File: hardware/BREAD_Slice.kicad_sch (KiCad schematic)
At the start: 15 parts, among them J1 Conn_01x10_Female, J2 I2C_01x04

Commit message: Initial commit
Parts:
- removed C1, C3, C4: 22uF, Capacitor_SMD:C_1206_3216Metric, symbol Device:C_Small
- removed C2: 100nF, Capacitor_SMD:C_1206_3216Metric, symbol Device:C_Small
- removed D1: WS2812B_5050, SparkFun-LED:WS2812-5050-4PIN, symbol SparkFun-LED:WS2812B_5050
- removed HS1: Heatsink_Pad, SparkFun-Fuse:Thermal Pad, symbol Mechanical:Heatsink_Pad
- removed J2: I2C_01x04, Connector_JST:JST_SH_SM04B-SRSS-TB_1x04-1MP_P1.00mm_Horizontal, symbol SparkFun-Connector:I2C_01x04
- removed L1: 4.7uH, Inductor_SMD:L_1210_3225Metric, symbol Device:L_Small
- removed U1: ~, Package_TO_SOT_SMD:TSOT-23-6, symbol SparkFun-DiscreteSemi:AP63205
- added C1, C2: 10uF_t, OCI_UPL_FOOTPRINTS:C_2312, symbol BREAD_Slice-rescue:10uF_t-OCI_UPL_2_Capacitors
- added J2, J3, J4, J5: Screw_Terminal_01x02, TerminalBlock_TE-Connectivity:TerminalBlock_TE_282834-2_1x02_P2.54mm_Horizontal, symbol Connector:Screw_Terminal_01x02
- added Logo1: Logo_Open_Hardware_Small, Symbol:OSHW-Symbol_6.7x6mm_SilkScreen, symbol Graphic:Logo_Open_Hardware_Small
- added U1, U2, U3, U4: ACS723xMATR-10AB, Package_SO:SOIC-16W_7.5x10.3mm_P1.27mm, symbol Sensor_Current:ACS723xMATR-10AB
- H1, H4: footprint MountingHole:MountingHole_5mm -> MountingHole:MountingHole_3.2mm_M3_DIN965_Pad
- H2: renamed from H3; footprint MountingHole:MountingHole_5mm -> MountingHole:MountingHole_3.2mm_M3_DIN965_Pad
- H3: renamed from H2; footprint MountingHole:MountingHole_5mm -> MountingHole:MountingHole_3.2mm_M3_DIN965_Pad
- J1: symbol Connector:Conn_01x10_Female -> BREAD_Slice-rescue:Conn_01x10_Female-Connector
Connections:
- net +12V: now also A1.30 (VIN), C1.1
- net +5V: now also C2.1, U1.10 (VCC), U2.10 (VCC), U3.10 (VCC), U4.10 (VCC)
- net GND: now also C1.2, C2.2, U1.11 (NC), U1.13 (BW_SEL), U1.14 (NC), U1.15 (GND), U2.11 (NC), U2.13 (BW_SEL), U2.14 (NC), U2.15 (GND), U3.11 (NC), U3.13 (BW_SEL), U3.14 (NC), U3.15 (GND), U4.11 (NC), U4.13 (BW_SEL), U4.14 (NC), U4.15 (GND)
- net CURR1: now reaches A1.19 (A0)
- net CURR1: now also U1.12 (VIOUT)
- net CURR2: now reaches A1.20 (A1)
- net CURR2: now also U3.12 (VIOUT)
- net CURR3: now reaches A1.21 (A2)
- net CURR3: now also U2.12 (VIOUT)
- net CURR4: now reaches A1.22 (A3)
- net CURR4: now also U4.12 (VIOUT)
- net LED: no longer names the net of A1.8 (D5)
- new net: J2.2 (Pin_2), U1.1 (IP+), U1.2 (IP+), U1.3 (IP+), U1.4 (IP+)
- new net: J2.1 (Pin_1), U1.5 (IP-), U1.6 (IP-), U1.7 (IP-), U1.8 (IP-)
- new net: J4.2 (Pin_2), U3.1 (IP+), U3.2 (IP+), U3.3 (IP+), U3.4 (IP+)
- new net: J4.1 (Pin_1), U3.5 (IP-), U3.6 (IP-), U3.7 (IP-), U3.8 (IP-)
- new net: J3.2 (Pin_2), U2.1 (IP+), U2.2 (IP+), U2.3 (IP+), U2.4 (IP+)
- new net: J3.1 (Pin_1), U2.5 (IP-), U2.6 (IP-), U2.7 (IP-), U2.8 (IP-)
- new net: J5.2 (Pin_2), U4.1 (IP+), U4.2 (IP+), U4.3 (IP+), U4.4 (IP+)
- new net: J5.1 (Pin_1), U4.5 (IP-), U4.6 (IP-), U4.7 (IP-), U4.8 (IP-)
- no-connect marks 22 -> 17
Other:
- moved on the sheet: A1, H1, H2, H3, H4, J1

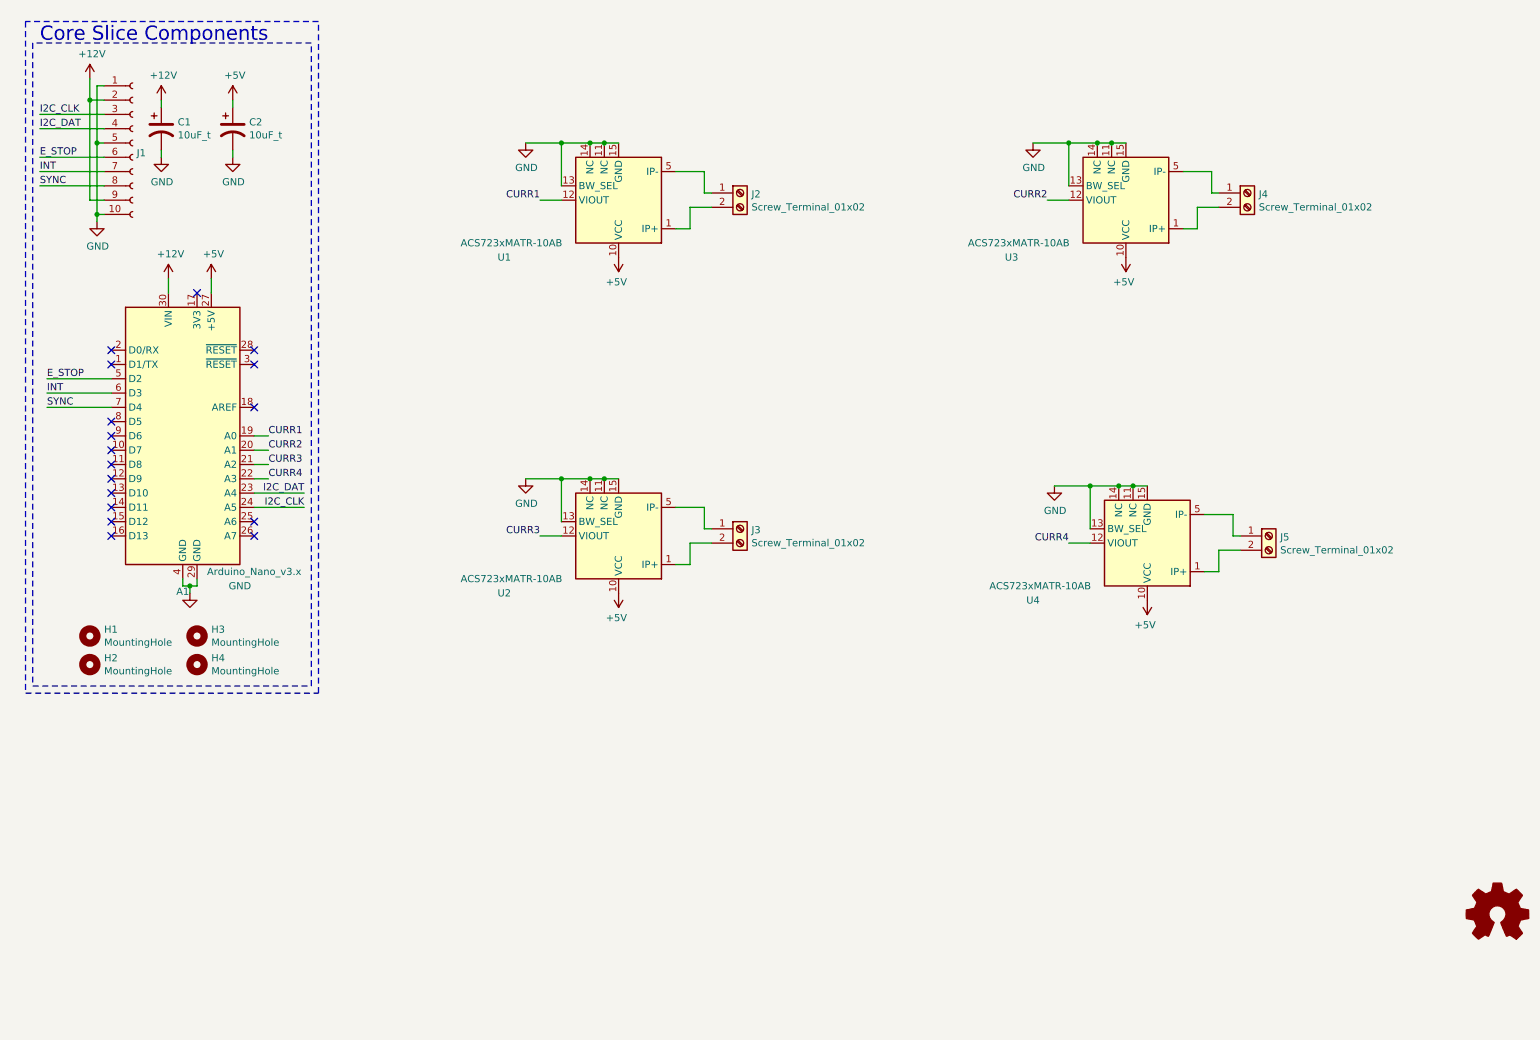
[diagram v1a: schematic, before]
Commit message: updated to new BREAD format
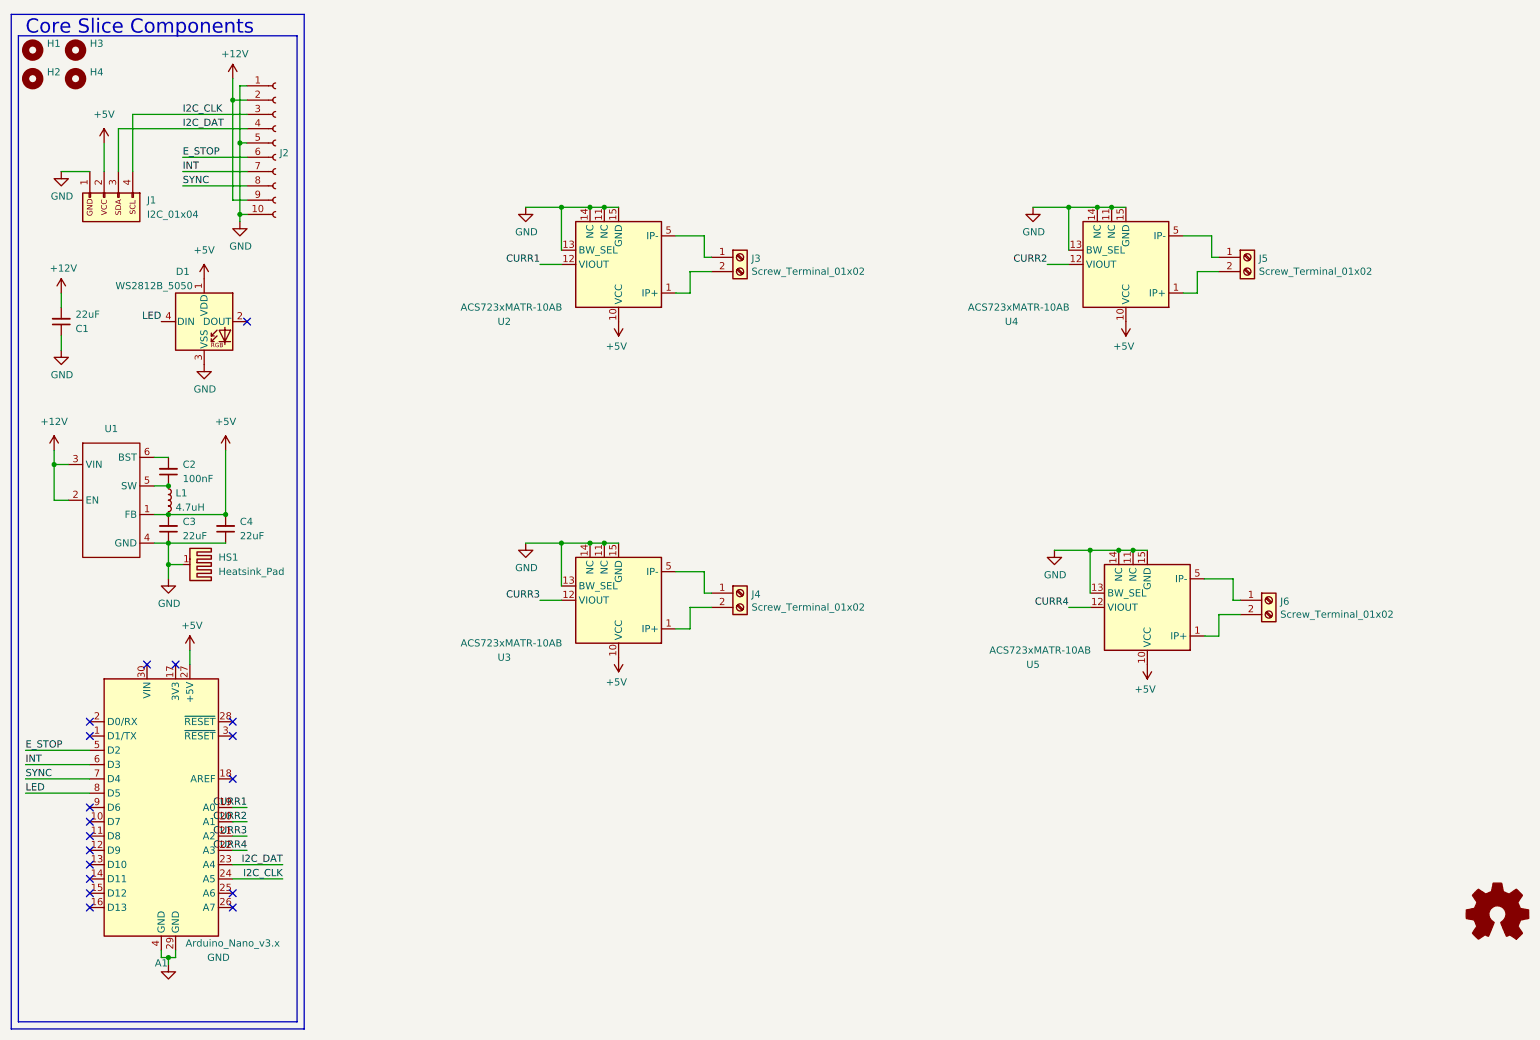
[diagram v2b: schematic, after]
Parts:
- removed C1, C2: 10uF_t, OCI_UPL_FOOTPRINTS:C_2312, symbol BREAD_Slice-rescue:10uF_t-OCI_UPL_2_Capacitors
- removed J2: Screw_Terminal_01x02, TerminalBlock_TE-Connectivity:TerminalBlock_TE_282834-2_1x02_P2.54mm_Horizontal, symbol Connector:Screw_Terminal_01x02
- removed Logo1: Logo_Open_Hardware_Small, Symbol:OSHW-Symbol_6.7x6mm_SilkScreen, symbol Graphic:Logo_Open_Hardware_Small
- removed U1: ACS723xMATR-10AB, Package_SO:SOIC-16W_7.5x10.3mm_P1.27mm, symbol Sensor_Current:ACS723xMATR-10AB
- added C1, C3, C4: 22uF, Capacitor_SMD:C_1206_3216Metric, symbol Device:C_Small
- added C2: 100nF, Capacitor_SMD:C_1206_3216Metric, symbol Device:C_Small
- added D1: WS2812B_5050, SparkFun-LED:WS2812-5050-4PIN, symbol SparkFun-LED:WS2812B_5050
- added HS1: Heatsink_Pad, KML-Custom:Thermal Pad, symbol Mechanical:Heatsink_Pad
- added J1: I2C_01x04, Connector_JST:JST_SH_SM04B-SRSS-TB_1x04-1MP_P1.00mm_Horizontal, symbol SparkFun-Connector:I2C_01x04
- added J6: Screw_Terminal_01x02, TerminalBlock_TE-Connectivity:TerminalBlock_TE_282834-2_1x02_P2.54mm_Horizontal, symbol Connector:Screw_Terminal_01x02
- added L1: 4.7uH, Inductor_SMD:L_1210_3225Metric, symbol Device:L_Small
- added U1: ~, Package_TO_SOT_SMD:TSOT-23-6, symbol SparkFun-DiscreteSemi:AP63205
- added U5: ACS723xMATR-10AB, Package_SO:SOIC-16W_7.5x10.3mm_P1.27mm, symbol Sensor_Current:ACS723xMATR-10AB
- H1, H4: footprint MountingHole:MountingHole_3.2mm_M3_DIN965_Pad -> MountingHole:MountingHole_5mm
- H2: renamed from H3; footprint MountingHole:MountingHole_3.2mm_M3_DIN965_Pad -> MountingHole:MountingHole_5mm
- H3: renamed from H2; footprint MountingHole:MountingHole_3.2mm_M3_DIN965_Pad -> MountingHole:MountingHole_5mm
- J2: renamed from J1; symbol BREAD_Slice-rescue:Conn_01x10_Female-Connector -> Connector:Conn_01x10_Female
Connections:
- net +12V: now also C1.2, U1.2 (EN), U1.3 (VIN); no longer A1.30 (VIN)
- net +5V: now also C3.2, C4.2, D1.1 (VDD), J1.2 (Pin_2), L1.2, U1.1 (FB), U5.10 (VCC)
- net CURR1: now also U2.12 (VIOUT)
- net CURR2: now also U4.12 (VIOUT); no longer U3.12 (VIOUT)
- net CURR3: now also U3.12 (VIOUT); no longer U2.12 (VIOUT)
- net CURR4: now also U5.12 (VIOUT); no longer U4.12 (VIOUT)
- net GND: now also C1.1, C3.1, C4.1, D1.3 (VSS), HS1.1, J1.1 (Pin_1), U1.4 (GND), U5.11 (NC), U5.13 (BW_SEL), U5.14 (NC), U5.15 (GND)
- net I2C_CLK: now also J1.4 (Pin_4)
- net I2C_DAT: now also J1.3 (Pin_3)
- net LED: now reaches A1.8 (D5)
- net LED: now also D1.4 (DIN)
- new net: C2.1, L1.1, U1.5 (SW)
- new net: C2.2, U1.6 (BST)
- new net: J6.1 (Pin_1), U5.5 (IP-), U5.6 (IP-), U5.7 (IP-), U5.8 (IP-)
- new net: J6.2 (Pin_2), U5.1 (IP+), U5.2 (IP+), U5.3 (IP+), U5.4 (IP+)
- no-connect marks 17 -> 18
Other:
- moved on the sheet: A1, H1, H2, H3, H4, J2

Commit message: updated for CRxx forking
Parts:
- J3, J4, J5, J6: footprint TerminalBlock_TE-Connectivity:TerminalBlock_TE_282834-2_1x02_P2.54mm_Horizontal -> CRx:Pheonix Conn Term TDPT 4 2-SP-6,35-ZB
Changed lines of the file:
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@@
 			)
 		)
-		(property "Footprint" "TerminalBlock_TE-Connectivity:TerminalBlock_TE_282834-2_1x02_P2.54mm_Horizontal"
+		(property "Footprint" "CRx:Pheonix Conn Term TDPT 4 2-SP-6,35-ZB"
 			(at 143.51 116.84 0)
 			(effects
@@
 			)
 		)
-		(property "Footprint" "TerminalBlock_TE-Connectivity:TerminalBlock_TE_282834-2_1x02_P2.54mm_Horizontal"
+		(property "Footprint" "CRx:Pheonix Conn Term TDPT 4 2-SP-6,35-ZB"
 			(at 237.49 118.11 0)
 			(effects
@@
 			)
 		)
-		(property "Footprint" "TerminalBlock_TE-Connectivity:TerminalBlock_TE_282834-2_1x02_P2.54mm_Horizontal"
+		(property "Footprint" "CRx:Pheonix Conn Term TDPT 4 2-SP-6,35-ZB"
 			(at 143.51 57.15 0)
 			(effects
@@
 			)
 		)
-		(property "Footprint" "TerminalBlock_TE-Connectivity:TerminalBlock_TE_282834-2_1x02_P2.54mm_Horizontal"
+		(property "Footprint" "CRx:Pheonix Conn Term TDPT 4 2-SP-6,35-ZB"
 			(at 233.68 57.15 0)
 			(effects
